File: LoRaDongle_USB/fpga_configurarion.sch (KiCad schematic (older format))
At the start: 12 parts

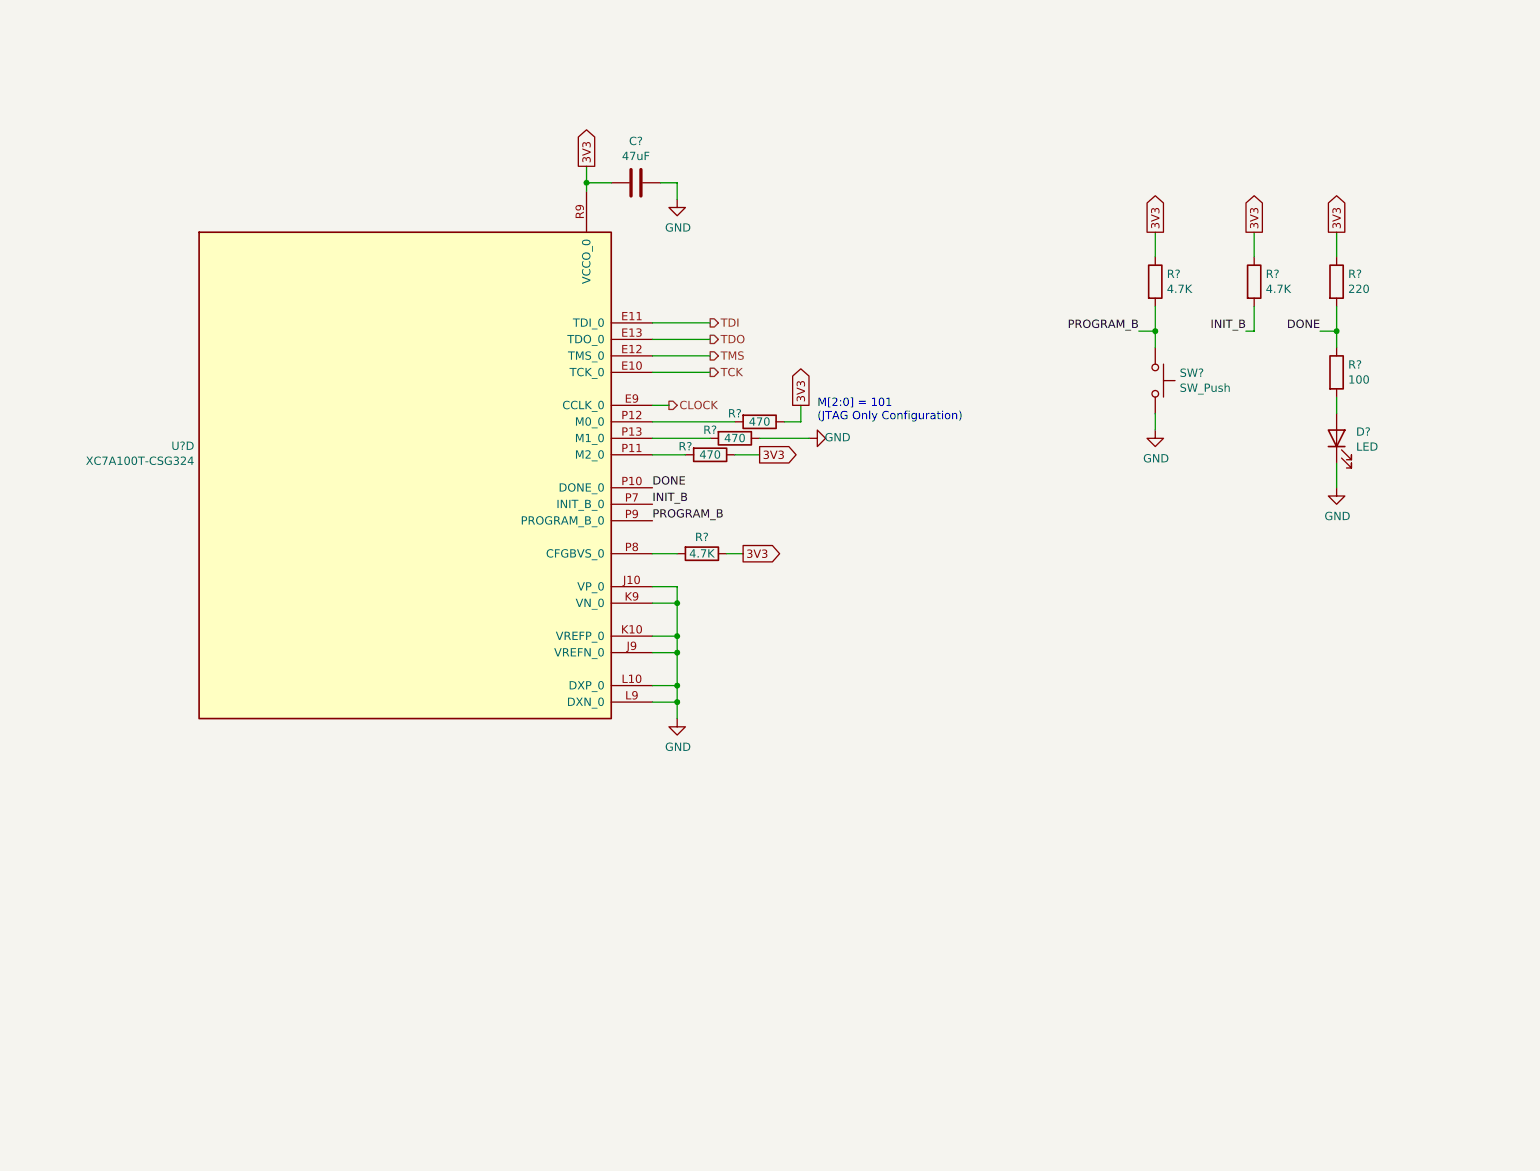
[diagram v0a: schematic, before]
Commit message: ft232h completed
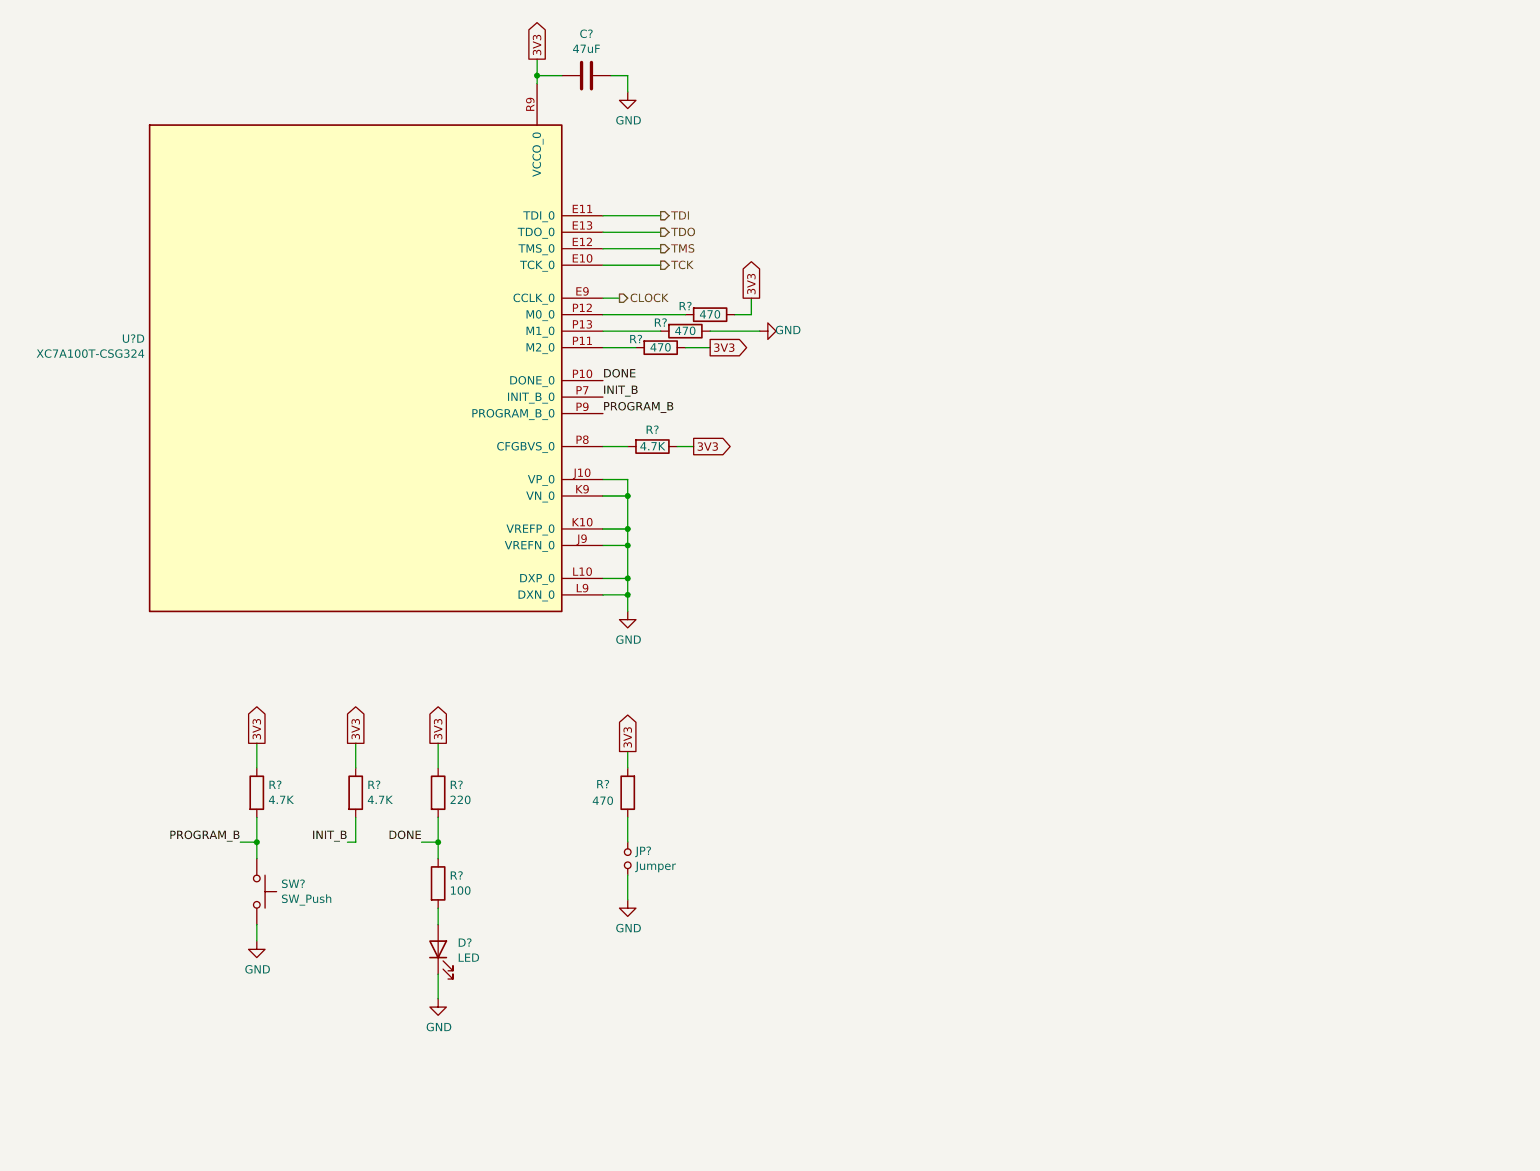
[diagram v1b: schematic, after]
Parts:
- added JP?: Jumper, symbol Device:Jumper_NO_Small
- added R?: 470, Resistor_SMD:R_0402_1005Metric, symbol Device:R
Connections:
- net 3V3: now also R?.2
- net GND: now also JP?.2
- new net: JP?.1, R?.1
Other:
- note removed: "M[2:0] = 101\n(JTAG Only Configuration)\n"
- moved on the sheet: C?, D?, R?, SW?, U?D

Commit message: added flash memory configuration
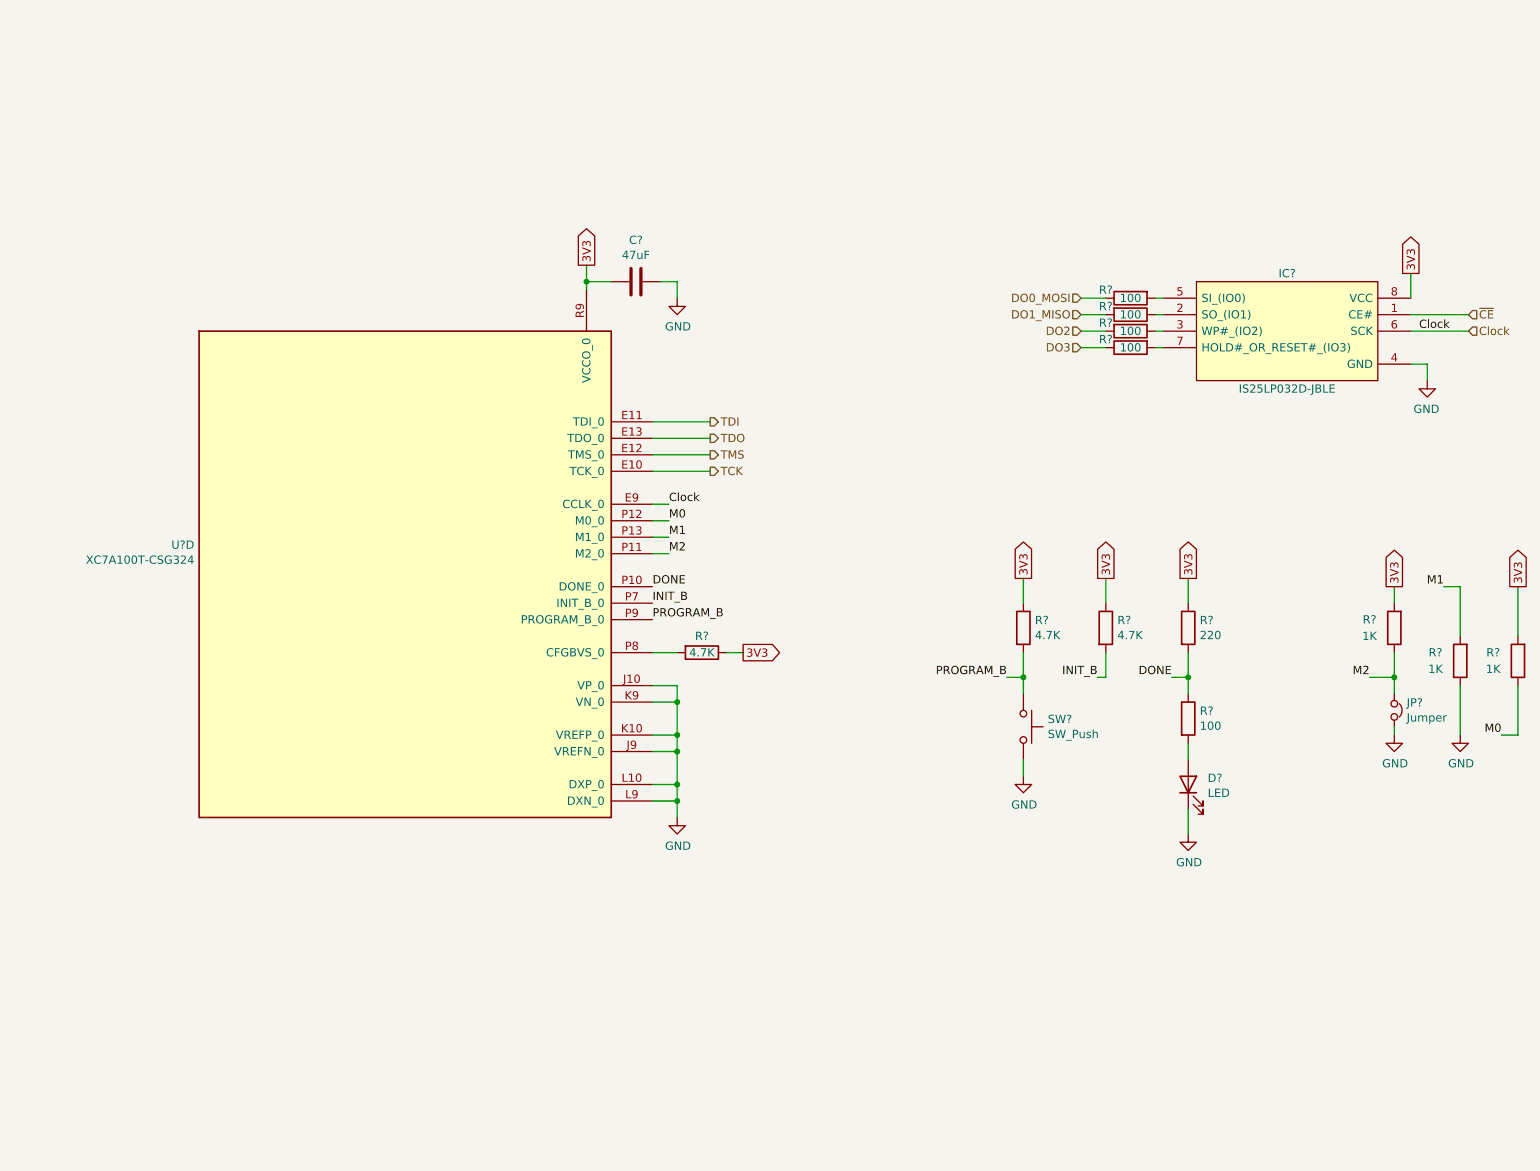
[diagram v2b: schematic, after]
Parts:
- removed JP?: Jumper, symbol Device:Jumper_NO_Small
- removed R? (x3): 470, Resistor_SMD:R_0402_1005Metric, symbol Device:R
- added IC?: IS25LP032D-JBLE, SOIC127P790X216-8N, symbol IS25LP032D-JBLE:IS25LP032D-JBLE
- added JP?: Jumper, symbol Device:Jumper_NC_Small
- added R? (x2): 1K, Resistor_SMD:R_0402_1005Metric, symbol Device:R
- added R? (x4): 100, Resistor_SMD:R_0402_1005Metric, symbol Device:R
- R?: value 470 -> 1K
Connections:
- net 3V3: now also IC?.8 (VCC), R?.2
- net GND: now also IC?.4 (GND), JP?.2, R?.1
- net M0: now reaches U?.P12 (M0_0)
- net M0: now also R?.1
- net M1: now reaches U?.P13 (M1_0)
- net M1: now also R?.2
- net M2: now reaches U?.P11 (M2_0)
- net M2: now also R?.1, JP?.1
- net CLOCK renamed Clock
- net Clock: now also IC?.6 (SCK)
- new net: IC?.2 (SO_(IO1)), R?.1
- new net: IC?.3 (WP#_(IO2)), R?.1
- new net: IC?.5 (SI_(IO0)), R?.2
- new net: IC?.7 (HOLD#_OR_RESET#_(IO3)), R?.2
- new net DO0_MOSI: R?.1
- new net DO1_MISO: R?.2
- new net DO2: R?.2
- new net DO3: R?.1
- new net ~CE: IC?.1 (CE#)
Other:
- moved on the sheet: C?, D?, R?, SW?, U?D

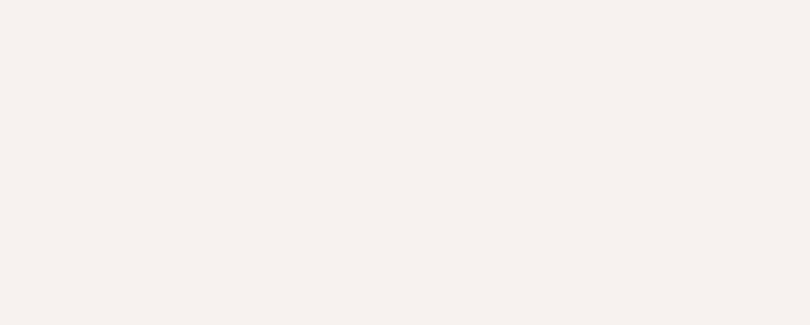
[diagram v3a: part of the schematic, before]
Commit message: updated with dip switch
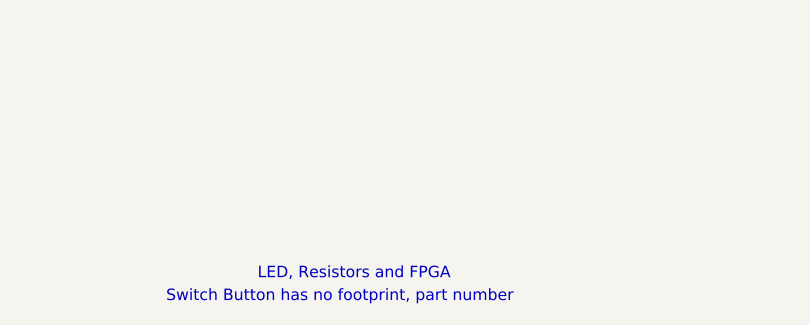
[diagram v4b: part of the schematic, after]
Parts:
- JP?: footprint (none) -> Connector_PinHeader_2.54mm:PinHeader_1x02_P2.54mm_Vertical
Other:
- note added: "LED, Resistors and FPGA"
- note added: "Switch Button has no footprint, part number"
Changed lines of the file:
@@
 $Descr A4 11693 8268
 encoding utf-8
-Sheet 5 7
+Sheet 6 7
 Title ""
 Date ""
@@
 F 0 "JP?" V 8904 4875 50  0000 L CNN
 F 1 "Jumper" V 8995 4875 50  0000 L CNN
-F 2 "" H 8950 4800 50  0001 C CNN
+F 2 "Connector_PinHeader_2.54mm:PinHeader_1x02_P2.54mm_Vertical" H 8950 4800 50  0001 C CNN
 F 3 "~" H 8950 4800 50  0001 C CNN
 	1    8950 4800
@@
 Wire Wire Line
 	9050 2500 9400 2500
+Text Notes 5450 7400 0    50   ~ 0
+LED, Resistors and FPGA
+Text Notes 5050 7500 0    50   ~ 0
+Switch Button has no footprint, part number
 $EndSCHEMATC
